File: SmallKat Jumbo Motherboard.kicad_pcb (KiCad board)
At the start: 4 copper layers, 80 x 80 mm, 49 parts, among them IC1 TPS562201DDCR, IC2 TPS562201DDCR, J1 Conn_01x06_Male, J10 Conn_01x06_Male, J11 Conn_01x06_Male, J12 Conn_01x04_Male, J13 Conn_01x02_Male, J14 Conn_01x04_Male, J15 Conn_01x04_Male, J16 Conn_01x06_Male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

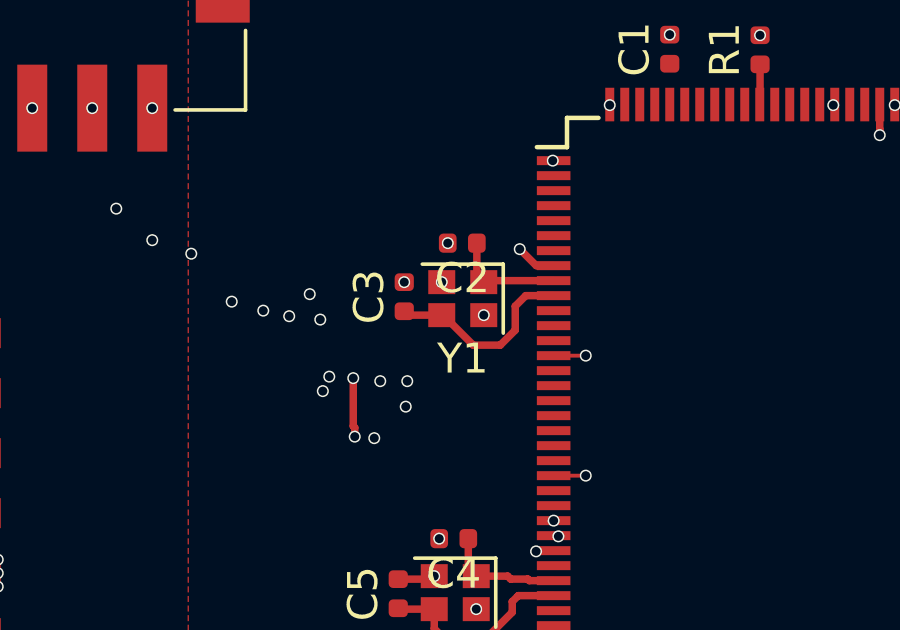
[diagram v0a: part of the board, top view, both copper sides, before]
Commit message: Changed footprints
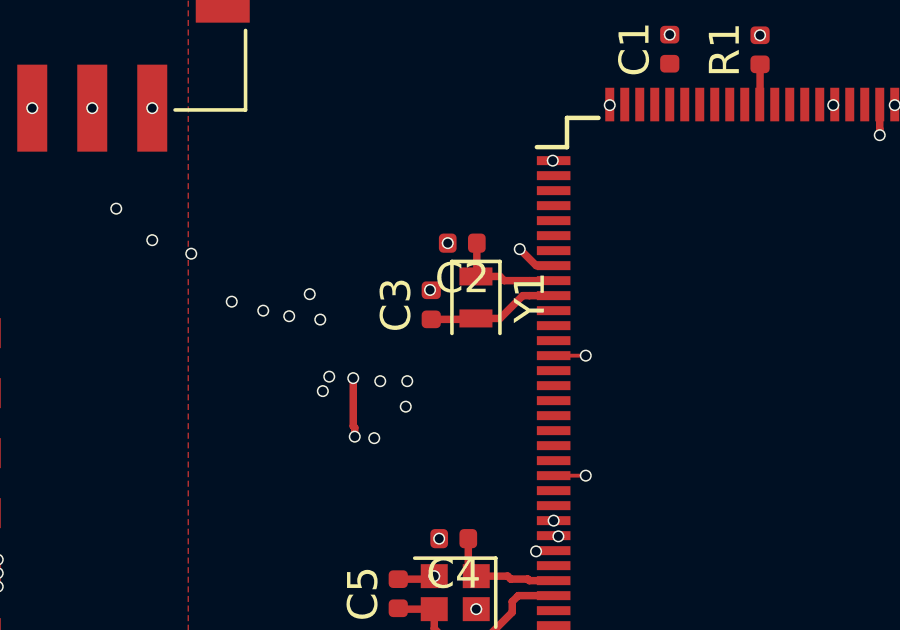
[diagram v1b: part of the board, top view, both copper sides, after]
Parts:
- C1: value C -> 1UF
- C10, C11, C16, C17: value C -> 0.1UF
- C12, C13, C6, C7: value C -> 22UF
- C14, C15, C8, C9: value C -> 10UF
- C2, C3, C4, C5: value C -> 10PF
- D1, D2: value D -> 641-1675-1-ND
- L1, L2: value L -> 4.7UH
- R1, R2, R3, R5, R6: value R -> 10K
- R4, R7: value R -> 33.2K
- Y1: value 32MHZ -> 32.768khz; footprint Crystal:Crystal_SMD_2016-4Pin_2.0x1.6mm -> Crystal:Crystal_SMD_2012-2Pin_2.0x1.2mm
- moved C3 0.94 mm to (23.3, 34.1)
- moved Y1 0.44 mm to (24.8, 33.8), turned to 270 degrees
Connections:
- Y1 pad 2: GND -> OSCOUT_32
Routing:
- net OSCOUT_32: track 6.60 -> 4.41 mm
- net GND: vias 311 -> 309
